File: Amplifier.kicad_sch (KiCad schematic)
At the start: 26 parts

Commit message: New power supply
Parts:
- gave numbers to parts that had none: 26

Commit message: New amplifier PCB
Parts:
- C10, C9: footprint Capacitor_THT:CP_Radial_D5.0mm_P2.00mm -> spdf1626_lib:C_THT_D5.0mm_P2.54mm
- C6, C7: footprint Capacitor_THT:C_Rect_L7.2mm_W3.0mm_P5.00mm_FKS2_FKP2_MKS2_MKP2 -> spdf1626_lib:C_THT_K73-17_P7.00mm
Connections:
- net GND: now also RV1.1; no longer RV1.3
- net at C6.2, C7.2: now also RV1.3; no longer RV1.1
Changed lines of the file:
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@@
     (property "Reference" "C7" (id 0) (at 127 104.14 90))
     (property "Value" "33n" (id 1) (at 127 106.68 90))
-    (property "Footprint" "Capacitor_THT:C_Rect_L7.2mm_W3.0mm_P5.00mm_FKS2_FKP2_MKS2_MKP2" (id 2) (at 132.08 111.4552 0)
+    (property "Footprint" "spdf1626_lib:C_THT_K73-17_P7.00mm" (id 2) (at 132.08 111.4552 0)
       (effects (font (size 1.27 1.27)) hide)
     )
@@
     (property "Reference" "C6" (id 0) (at 127 80.01 90))
     (property "Value" "33n opt" (id 1) (at 127 77.47 90))
-    (property "Footprint" "Capacitor_THT:C_Rect_L7.2mm_W3.0mm_P5.00mm_FKS2_FKP2_MKS2_MKP2" (id 2) (at 132.08 72.6948 0)
+    (property "Footprint" "spdf1626_lib:C_THT_K73-17_P7.00mm" (id 2) (at 132.08 72.6948 0)
       (effects (font (size 1.27 1.27)) hide)
     )
@@
       (effects (font (size 1.27 1.27)) (justify left))
     )
-    (property "Footprint" "Capacitor_THT:CP_Radial_D5.0mm_P2.00mm" (id 2) (at 180.0352 57.15 0)
+    (property "Footprint" "spdf1626_lib:C_THT_D5.0mm_P2.54mm" (id 2) (at 180.0352 57.15 0)
       (effects (font (size 1.27 1.27)) hide)
     )
@@
       (effects (font (size 1.27 1.27)) (justify left))
     )
-    (property "Footprint" "Capacitor_THT:CP_Radial_D5.0mm_P2.00mm" (id 2) (at 191.4652 57.15 0)
+    (property "Footprint" "spdf1626_lib:C_THT_D5.0mm_P2.54mm" (id 2) (at 191.4652 57.15 0)
       (effects (font (size 1.27 1.27)) hide)
     )
@@
     (pin "1")
   )
-  (symbol (lib_id "Device:R_Potentiometer") (at 135.89 118.11 0) (unit 1)
+  (symbol (lib_id "Device:R_Potentiometer") (at 135.89 118.11 0) (mirror x) (unit 1)
     (in_bom yes) (on_board yes) (fields_autoplaced)
     (property "Reference" "RV1" (id 0) (at 133.35 116.8399 0)
@@
     (pin "2")
   )
+  (sheet_instances
+    (path "/" (page "1"))
+  )
+  (symbol_instances
+    (path "/7d354e65-c937-4b8d-b990-6e217875a5de"
+      (reference "#PWR01") (unit 1) (value "GND") (footprint "")
+    )
+    (path "/ab08fae4-ea99-4f34-b35f-30bf8021c06c"
+      (reference "#PWR02") (unit 1) (value "GND") (footprint "")
+    )
+    (path "/7e3d583d-62e1-4605-9dc6-eb3de477f996"
+      (reference "#PWR03") (unit 1) (value "GND") (footprint "")
+    )
+    (path "/3cd04640-8481-49c0-8bbd-54748a44f75a"
+      (reference "#PWR04") (unit 1) (value "+6V") (footprint "")
+    )
+    (path "/98ee1497-597e-4d9e-9132-87a133f2a09f"
+      (reference "#PWR05") (unit 1) (value "GND") (footprint "")
+    )
+    (path "/81f52771-8a53-4346-bb7f-a78b76ca4610"
+      (reference "#PWR06") (unit 1) (value "GND") (footprint "")
+    )
+    (path "/96d9451e-589a-4a1e-ba29-92a8936115b0"
+      (reference "#PWR07") (unit 1) (value "+6V") (footprint "")
+    )
+    (path "/5b2b1ce9-93e8-42a4-8559-904140854f90"
+      (reference "#PWR08") (unit 1) (value "GND") (footprint "")
+    )
+    (path "/38cf8442-d772-418c-8ff7-8770aea5510f"
+      (reference "#PWR09") (unit 1) (value "GND") (footprint "")
+    )
+    (path "/26756bad-7f8e-4771-8d83-1b031173000d"
+      (reference "#PWR010") (unit 1) (value "GND") (footprint "")
+    )
+    (path "/ee8a1838-4bfe-42c4-9035-0143c23875e3"
+      (reference "#PWR011") (unit 1) (value "GND") (footprint "")
+    )
+    (path "/febfe4f1-2973-49da-883e-4d951957227e"
+      (reference "#PWR012") (unit 1) (value "GND") (footprint "")
+    )
+    (path "/4bf0dee3-3a1e-4215-a58b-115fac657302"
+      (reference "#PWR013") (unit 1) (value "+6V") (footprint "")
+    )
+    (path "/ca133b91-1921-458a-8ce5-d49e060f9811"
+      (reference "#PWR014") (unit 1) (value "GND") (footprint "")
+    )
+    (path "/826af9cc-568a-4736-b3fe-abd787b69b20"
+      (reference "#PWR015") (unit 1) (value "+6V") (footprint "")
+    )
+    (path "/8d172b20-b1ee-4fbd-8ac9-b046d96cbd61"
+      (reference "#PWR016") (unit 1) (value "GND") (footprint "")
+    )
+    (path "/f1acec99-e5fd-4667-b36f-d7e14eeea182"
+      (reference "C2") (unit 1) (value "100n") (footprint "spdf1626_lib:C_THT_K73-17_P9.00mm")
+    )
+    (path "/f671337d-0862-4107-b7ac-3d710e374714"
+      (reference "C3") (unit 1) (value "1n") (footprint "spdf1626_lib:C_THT_K73-17_P5.00mm")
+    )
+    (path "/60a6b14b-e979-43aa-815a-7d25c2bc9385"
+      (reference "C4") (unit 1) (value "10uF") (footprint "spdf1626_lib:C_THT_D10.0mm_P5.00mm")
+    )
+    (path "/4b7b5fb2-6349-4007-ba90-c3ac2e2c6584"
+      (reference "C5") (unit 1) (value "100n") (footprint "spdf1626_lib:C_THT_K73-17_P9.00mm")
+    )
+    (path "/449c9898-71f5-47a5-bc1c-95f5c5e04a52"
+      (reference "C6") (unit 1) (value "33n opt") (footprint "spdf1626_lib:C_THT_K73-17_P7.00mm")
+    )
+    (path "/42ef9186-4184-4466-b743-ee5971dcf03c"
+      (reference "C7") (unit 1) (value "33n") (footprint "spdf1626_lib:C_THT_K73-17_P7.00mm")
+    )
+    (path "/f91c3ef0-e986-4110-b1f4-2b0562b8580a"
+      (reference "C8") (unit 1) (value "10uF") (footprint "spdf1626_lib:C_THT_D10.0mm_P5.00mm")
+    )
+    (path "/68e0188b-48a6-4a9c-b99a-2eedbba297c5"
+      (reference "C9") (unit 1) (value "10uF") (footprint "spdf1626_lib:C_THT_D5.0mm_P2.54mm")
+    )
+    (path "/95fee9cb-3e70-47a8-92fa-234d16b7b1f8"
+      (reference "C10") (unit 1) (value "10uF") (footprint "spdf1626_lib:C_THT_D5.0mm_P2.54mm")
+    )
+    (path "/f32711b0-8890-487d-94d6-c1716e399909"
+      (reference "J1") (unit 1) (value "Input") (footprint "spdf1626_lib:PinHeader_1x02_P2.54mm")
+    )
+    (path "/4fce7e63-e341-4b44-a9d1-300f40523c0b"
+      (reference "J2") (unit 1) (value "Conn_01x04") (footprint "spdf1626_lib:PinHeader_1x04_P2.54mm")
+    )
+    (path "/ffec4411-a16b-4d16-b464-4f2a70d85e6e"
+      (reference "J3") (unit 1) (value "output") (footprint "spdf1626_lib:PinHeader_1x02_P2.54mm")
+    )
+    (path "/d65b55e5-95fa-499a-a3b7-061e47ad87ef"
+      (reference "R1") (unit 1) (value "300k") (footprint "spdf1626_lib:R_THT_025W")
+    )
+    (path "/7f2e2995-3c2f-40af-9329-1944979bc940"
+      (reference "R2") (unit 1) (value "200R") (footprint "spdf1626_lib:R_THT_025W")
+    )
+    (path "/2f22f7f4-6d56-45f4-ae15-bf2406f9ea65"
+      (reference "R3") (unit 1) (value "1k8") (footprint "spdf1626_lib:R_THT_025W")
+    )
+    (path "/455c7ae2-abcf-4660-9c0f-f321d087ff4b"
+      (reference "R4") (unit 1) (value "220k opt") (footprint "spdf1626_lib:R_THT_025W")
+    )
+    (path "/98fb5eca-9e6c-44e3-8a7b-0b480d935f00"
+      (reference "R5") (unit 1) (value "680R") (footprint "spdf1626_lib:R_THT_025W")
+    )
+    (path "/0e76d439-f46c-427c-8210-4ea36a5ac58f"
+      (reference "R6") (unit 1) (value "300k") (footprint "spdf1626_lib:R_THT_025W")
+    )
+    (path "/b6b53ef3-dbf2-4a41-8117-119e97e62d98"
+      (reference "R7") (unit 1) (value "200R") (footprint "spdf1626_lib:R_THT_025W")
+    )
+    (path "/0e932ddd-4c58-4362-9fa3-dc371042746a"
+      (reference "R8") (unit 1) (value "1k8") (footprint "spdf1626_lib:R_THT_025W")
+    )
+    (path "/e245ac41-1fa2-432f-a1cb-9c74b374dfc2"
+      (reference "R9") (unit 1) (value "6k8") (footprint "spdf1626_lib:R_THT_025W")
+    )
+    (path "/4f6647a6-5733-446e-b069-0fe4ef4b4964"
+      (reference "R10") (unit 1) (value "220R*") (footprint "spdf1626_lib:R_THT_1W")
+    )
+    (path "/ae3ecd0c-cf09-4e21-bebe-5c96905c14b0"
+      (reference "RV1") (unit 1) (value "100k") (footprint "spdf1626_lib:Potentiometer_THT_CA9V")
+    )
+    (path "/57e9c211-456f-4120-9b3a-03f62ecda79d"
+      (reference "T1") (unit 1) (value "Transformer_SP_1S") (footprint "spdf1626_lib:Output_transformer")
+    )
+    (path "/3b4b5ffe-6bc0-419a-87c0-3add445964f4"
+      (reference "U1") (unit 1) (value "6N2P") (footprint "spdf1626_lib:9-pin_tube_socket")
+    )
+    (path "/7fdc7ecf-516c-4b8a-829e-19c8463e595a"
+      (reference "U2") (unit 1) (value "6P14P") (footprint "spdf1626_lib:9-pin_tube_socket")
+    )
+  )
 )

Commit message: Neon bulb added on the amplifier PCB
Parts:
- added J4: Neon bulb, spdf1626_lib:PinHeader_1x02_P2.54mm, symbol Connector_Generic:Conn_01x02
- added R11: 1M, spdf1626_lib:R_THT_025W, symbol Device:R
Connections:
- net 240V: now also R11.2
- net GND: now also J4.2 (Pin_2)
- new net: J4.1 (Pin_1), R11.1
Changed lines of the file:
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@@
+    (stroke (width 0) (type default) (color 0 0 0 0))
+  )
+  (wire (pts (xy 52.07 74.93) (xy 52.07 72.39))
     (stroke (width 0) (type default) (color 0 0 0 0))
   )
@@
     (stroke (width 0) (type default) (color 0 0 0 0))
   )
+  (wire (pts (xy 52.07 72.39) (xy 49.53 72.39))
+    (stroke (width 0) (type default) (color 0 0 0 0))
+  )
+  (wire (pts (xy 52.07 57.15) (xy 52.07 59.69))
+    (stroke (width 0) (type default) (color 0 0 0 0))
+  )
   (wire (pts (xy 170.18 111.76) (xy 170.18 114.3))
     (stroke (width 0) (type default) (color 0 0 0 0))
@@
     (stroke (width 0) (type default) (color 0 0 0 0))
   )
+  (wire (pts (xy 52.07 69.85) (xy 52.07 67.31))
+    (stroke (width 0) (type default) (color 0 0 0 0))
+  )
   (wire (pts (xy 125.73 50.8) (xy 125.73 45.72))
     (stroke (width 0) (type default) (color 0 0 0 0))
@@
     (stroke (width 0) (type default) (color 0 0 0 0))
   )
+  (wire (pts (xy 49.53 69.85) (xy 52.07 69.85))
+    (stroke (width 0) (type default) (color 0 0 0 0))
+  )
   (wire (pts (xy 90.17 80.01) (xy 90.17 86.36))
     (stroke (width 0) (type default) (color 0 0 0 0))
@@
   (wire (pts (xy 215.9 77.47) (xy 218.44 77.47))
     (stroke (width 0) (type default) (color 0 0 0 0))
+  )
+  (global_label "240V" (shape input) (at 52.07 57.15 90) (fields_autoplaced)
+    (effects (font (size 1.27 1.27)) (justify left))
+    (property "Обозначения листов" "${INTERSHEET_REFS}" (id 0) (at 51.9906 50.0198 90)
+      (effects (font (size 1.27 1.27)) (justify left) hide)
+    )
   )
   (global_label "240V" (shape input) (at 121.92 53.34 180) (fields_autoplaced)
@@
     (pin "1")
     (pin "2")
+  )
+  (symbol (lib_id "power:GND") (at 52.07 74.93 0) (unit 1)
+    (in_bom yes) (on_board yes) (fields_autoplaced)
+    (property "Reference" "#PWR017" (id 0) (at 52.07 81.28 0)
+      (effects (font (size 1.27 1.27)) hide)
+    )
+    (property "Value" "GND" (id 1) (at 52.07 80.01 0))
+    (property "Footprint" "" (id 2) (at 52.07 74.93 0)
+      (effects (font (size 1.27 1.27)) hide)
+    )
+    (property "Datasheet" "" (id 3) (at 52.07 74.93 0)
+      (effects (font (size 1.27 1.27)) hide)
+    )
+    (pin "1")
   )
   (symbol (lib_id "power:GND") (at 154.94 62.23 0) (unit 1)
@@
     (pin "4")
   )
+  (symbol (lib_id "Connector_Generic:Conn_01x02") (at 44.45 69.85 0) (mirror y) (unit 1)
+    (in_bom yes) (on_board yes) (fields_autoplaced)
+    (property "Reference" "J4" (id 0) (at 44.45 63.5 0))
+    (property "Value" "Neon bulb" (id 1) (at 44.45 66.04 0))
+    (property "Footprint" "spdf1626_lib:PinHeader_1x02_P2.54mm" (id 2) (at 44.45 69.85 0)
+      (effects (font (size 1.27 1.27)) hide)
+    )
+    (property "Datasheet" "~" (id 3) (at 44.45 69.85 0)
+      (effects (font (size 1.27 1.27)) hide)
+    )
+    (pin "1")
+    (pin "2")
+  )
   (symbol (lib_id "Device:Transformer_SP_1S") (at 201.93 82.55 0) (unit 1)
     (in_bom yes) (on_board yes) (fields_autoplaced)
@@
     (pin "1")
   )
+  (symbol (lib_id "Device:R") (at 52.07 63.5 180) (unit 1)
+    (in_bom yes) (on_board yes)
+    (property "Reference" "R11" (id 0) (at 54.61 62.23 0)
+      (effects (font (size 1.27 1.27)) (justify right))
+    )
+    (property "Value" "1M" (id 1) (at 54.61 64.77 0)
+      (effects (font (size 1.27 1.27)) (justify right))
+    )
+    (property "Footprint" "spdf1626_lib:R_THT_025W" (id 2) (at 53.848 63.5 90)
+      (effects (font (size 1.27 1.27)) hide)
+    )
+    (property "Datasheet" "~" (id 3) (at 52.07 63.5 0)
+      (effects (font (size 1.27 1.27)) hide)
+    )
+    (pin "1")
+    (pin "2")
+  )
   (symbol (lib_id "Device:C") (at 60.96 95.25 90) (mirror x) (unit 1)
     (in_bom yes) (on_board yes)
@@
       (reference "#PWR016") (unit 1) (value "GND") (footprint "")
     )
+    (path "/239bd0c1-7d24-40b1-8ecd-85f82d90c459"
+      (reference "#PWR017") (unit 1) (value "GND") (footprint "")
+    )
     (path "/f1acec99-e5fd-4667-b36f-d7e14eeea182"
       (reference "C2") (unit 1) (value "100n") (footprint "spdf1626_lib:C_THT_K73-17_P9.00mm")
@@
       (reference "J3") (unit 1) (value "output") (footprint "spdf1626_lib:PinHeader_1x02_P2.54mm")
     )
+    (path "/4ff71e44-dddb-450e-9f6f-fe3947968fd4"
+      (reference "J4") (unit 1) (value "Neon bulb") (footprint "spdf1626_lib:PinHeader_1x02_P2.54mm")
+    )
     (path "/d65b55e5-95fa-499a-a3b7-061e47ad87ef"
       (reference "R1") (unit 1) (value "300k") (footprint "spdf1626_lib:R_THT_025W")
@@
       (reference "R10") (unit 1) (value "220R*") (footprint "spdf1626_lib:R_THT_1W")
     )
+    (path "/ee8bc577-8a80-4c3d-a67d-e6eec779095a"
+      (reference "R11") (unit 1) (value "1M") (footprint "spdf1626_lib:R_THT_025W")
+    )
     (path "/ae3ecd0c-cf09-4e21-bebe-5c96905c14b0"

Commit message: Temp
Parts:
- removed J3: output, spdf1626_lib:PinHeader_1x02_P2.54mm, symbol Connector_Generic:Conn_01x02
- removed T1: Transformer_SP_1S, spdf1626_lib:Output_transformer, symbol Device:Transformer_SP_1S
- added C1: 10uF, spdf1626_lib:C_THT_D10.0mm_P5.00mm, symbol Device:C
- added J3: Transformer, spdf1626_lib:PinHeader_1x03_P2.54mm, symbol Connector_Generic:Conn_01x03
- J2: value Conn_01x04 -> Power; footprint spdf1626_lib:PinHeader_1x04_P2.54mm -> spdf1626_lib:MCV_1,5_4-G-3.5_1x04_P3.50mm_Vertical
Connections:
- net 240V: now also J3.1 (Pin_1)
- net GND: now also C1.2
- net at R10.1, U2.3: now also C1.1
- net at U2.9: now also J3.2 (Pin_2)
- net at U2.7: now also J3.3 (Pin_3)
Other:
- moved on the sheet: R9, U2

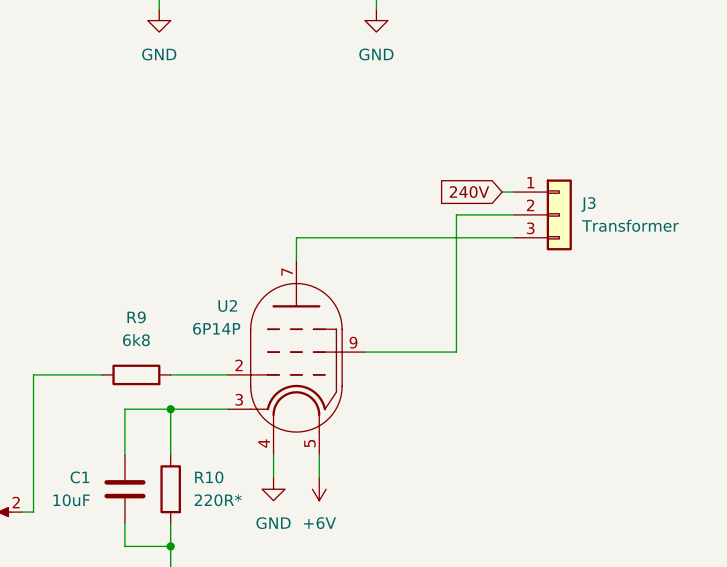
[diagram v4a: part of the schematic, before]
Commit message: New amplifier PCB with external transformer
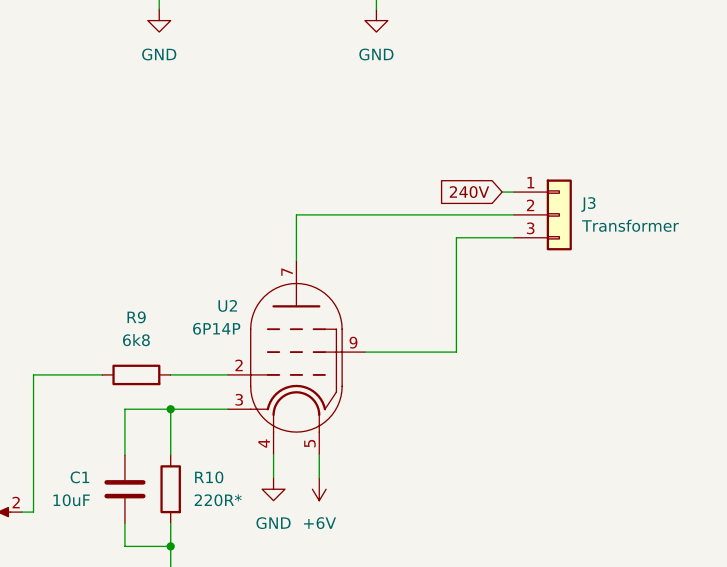
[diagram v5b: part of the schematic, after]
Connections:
- net at U2.7: now also J3.2 (Pin_2); no longer J3.3 (Pin_3)
- net at U2.9: now also J3.3 (Pin_3); no longer J3.2 (Pin_2)
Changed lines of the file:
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@@
     (stroke (width 0) (type default) (color 0 0 0 0))
   )
-  (wire (pts (xy 187.96 85.09) (xy 194.31 85.09))
+  (wire (pts (xy 187.96 87.63) (xy 194.31 87.63))
     (stroke (width 0) (type default) (color 0 0 0 0))
   )
@@
     (stroke (width 0) (type default) (color 0 0 0 0))
   )
-  (wire (pts (xy 170.18 87.63) (xy 194.31 87.63))
+  (wire (pts (xy 170.18 85.09) (xy 194.31 85.09))
     (stroke (width 0) (type default) (color 0 0 0 0))
   )
@@
     (stroke (width 0) (type default) (color 0 0 0 0))
   )
-  (wire (pts (xy 170.18 87.63) (xy 170.18 90.17))
+  (wire (pts (xy 170.18 85.09) (xy 170.18 90.17))
     (stroke (width 0) (type default) (color 0 0 0 0))
   )
@@
     (stroke (width 0) (type default) (color 0 0 0 0))
   )
-  (wire (pts (xy 187.96 85.09) (xy 187.96 100.33))
-    (stroke (width 0) (type default) (color 0 0 0 0))
-  )
+  (wire (pts (xy 187.96 87.63) (xy 187.96 100.33))
+    (stroke (width 0) (type default) (color 0 0 0 0))
+  )

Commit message: Hybrid Amplifier
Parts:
- removed J3: Transformer, spdf1626_lib:PinHeader_1x03_P2.54mm, symbol Connector_Generic:Conn_01x03
- added J3: Output, spdf1626_lib:PinHeader_1x02_P2.54mm, symbol Connector_Generic:Conn_01x02
- added T1: Transformer_SP_1S, spdf1626_lib:Output_transformer, symbol Device:Transformer_SP_1S
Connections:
- net 240V: now also T1.1 (PR1)
- net GND: now also J3.2 (Pin_2), T1.4 (S1)
- net at U2.7: now also T1.2 (PM)
- net at U2.9: now also T1.3 (PR2)
- new net: J3.1 (Pin_1), T1.5 (S2)
